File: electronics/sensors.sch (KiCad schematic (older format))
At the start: 11 parts, among them U3 MPU-9250, U4 MS5611-01BA, U5 VL53L0X

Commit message: Use wifi for telemetry
Cleanup schematic
Use ESP12E (wifi) for telemetry instead of NRF24
Reannotate & replot pdf
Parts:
- renumbered C14 to C16, C15 to C17, C17 to C20, C16 to C21, R18 to R16, U3 to U4, U4 to U5, U5 to U6
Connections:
- net MPU9250_CS renamed IMU_CS
- net MPU9250_INT renamed IMU_INT
- net SPI1_MISO renamed IMU_MISO
- net SPI1_MOSI renamed IMU_MOSI
- net SPI1_SCK renamed IMU_SCK
- net ST_VL53L0X_GPIO1 renamed TOF_GPIO1
- net ST_VL53L0X_XSHUT renamed TOF_XSHUT
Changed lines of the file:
@@
 $Descr A4 11693 8268
 encoding utf-8
-Sheet 2 4
+Sheet 2 3
 Title "Speedy the nanocopter"
-Date "2016-06-04"
-Rev "1E"
+Date "2016-06-24"
+Rev "1F"
 Comp "Salah-Eddine Missri"
 Comment1 "License: CC-BY 4.0"
@@
 	1    0    0    -1
 $EndComp
-Text HLabel 3425 2125 2    39   Input ~ 0
-SPI1_SCK
-Text HLabel 3425 2225 2    39   Input ~ 0
-SPI1_MOSI
-Text HLabel 3425 2375 2    39   Input ~ 0
-SPI1_MISO
-Text HLabel 3425 2525 2    39   Input ~ 0
-MPU9250_CS
-Text HLabel 3425 2675 2    39   Input ~ 0
-MPU9250_INT
-$Comp
-L MS5611-01BA U4
+Text HLabel 3375 2125 2    39   Input ~ 0
+IMU_SCK
+Text HLabel 3375 2225 2    39   Input ~ 0
+IMU_MOSI
+Text HLabel 3375 2375 2    39   Input ~ 0
+IMU_MISO
+Text HLabel 3375 2525 2    39   Input ~ 0
+IMU_CS
+Text HLabel 3375 2675 2    39   Input ~ 0
+IMU_INT
+$Comp
+L MS5611-01BA U5
 U 1 1 553861F3
 P 5975 2525
-F 0 "U4" H 6325 2925 50  0000 C CNN
+F 0 "U5" H 6325 2925 50  0000 C CNN
 F 1 "MS5611-01BA" H 5825 2925 50  0000 C CNN
 F 2 "_sensors:_MS5611-01BA" H 5975 2525 50  0001 C CNN
@@
 NoConn ~ 1775 2425
 $Comp
-L C_Small C14
+L C_Small C16
 U 1 1 554288B9
 P 1275 2025
-F 0 "C14" H 1285 2095 50  0000 L CNN
+F 0 "C16" H 1285 2095 50  0000 L CNN
 F 1 "0.1uF" H 1285 1945 50  0000 L CNN
 F 2 "_std:_0402" H 1275 2025 60  0001 C CNN
@@
 $EndComp
 $Comp
-L C_Small C15
+L C_Small C17
 U 1 1 55428A44
 P 1525 2025
-F 0 "C15" H 1535 2095 50  0000 L CNN
+F 0 "C17" H 1535 2095 50  0000 L CNN
 F 1 "10nF" H 1535 1945 50  0000 L CNN
 F 2 "_std:_0402" H 1525 2025 60  0001 C CNN
@@
 $EndComp
 $Comp
-L C_Small C16
+L C_Small C21
 U 1 1 55428B56
 P 3750 2875
-F 0 "C16" H 3760 2945 50  0000 L CNN
+F 0 "C21" H 3760 2945 50  0000 L CNN
 F 1 "0.1uF" H 3760 2795 50  0000 L CNN
 F 2 "_std:_0402" H 3750 2875 60  0001 C CNN
@@
 $EndComp
 $Comp
-L C_Small C17
+L C_Small C20
 U 1 1 55428C9E
 P 4975 2575
-F 0 "C17" H 4985 2645 50  0000 L CNN
+F 0 "C20" H 4985 2645 50  0000 L CNN
 F 1 "0.1uF" H 4985 2495 50  0000 L CNN
 F 2 "_std:_0402" H 4975 2575 60  0001 C CNN
@@
 	3750 2775 3375 2775
 Wire Wire Line
-	3425 2375 3375 2375
-Wire Wire Line
-	3425 2525 3375 2525
-Wire Wire Line
-	3425 2225 3375 2225
-Wire Wire Line
-	3425 2125 3375 2125
-Wire Wire Line
-	3425 2675 3375 2675
-Wire Wire Line
-	9900 2750 10250 2750
-Wire Wire Line
-	9900 2650 10250 2650
+	3375 2375 3375 2375
+Wire Wire Line
+	3375 2525 3375 2525
+Wire Wire Line
+	3375 2225 3375 2225
+Wire Wire Line
+	3375 2125 3375 2125
+Wire Wire Line
+	3375 2675 3375 2675
+Wire Wire Line
+	9900 2750 9900 2750
+Wire Wire Line
+	9900 2650 9900 2650
 Wire Wire Line
 	4975 2675 4975 2750
@@
 	5175 2425 5175 2325
 Wire Wire Line
-	6775 2425 6725 2425
-Wire Wire Line
-	6725 2325 6775 2325
+	6725 2425 6725 2425
+Wire Wire Line
+	6725 2325 6725 2325
 Wire Wire Line
 	6725 2725 6775 2725
@@
 Text Notes 3350 950  0    60   ~ 0
 IMU 10dof
-Text HLabel 6775 2325 2    39   Input ~ 0
+Text HLabel 6725 2325 2    39   Input ~ 0
 I2C1_SCL
-Text HLabel 6775 2425 2    39   Input ~ 0
+Text HLabel 6725 2425 2    39   Input ~ 0
 I2C1_SDA
-Text HLabel 10250 2750 2    39   Input ~ 0
+Text HLabel 9900 2750 2    39   Input ~ 0
 I2C1_SCL
-Text HLabel 10250 2650 2    39   Input ~ 0
+Text HLabel 9900 2650 2    39   Input ~ 0
 I2C1_SDA
 NoConn ~ 1775 3225
@@
 	3375 2875 3625 2875
 $Comp
-L MPU-9250 U3
+L MPU-9250 U4
 U 1 1 56ACAF9A
 P 2575 2525
-F 0 "U3" H 2575 3462 60  0000 C CNN
+F 0 "U4" H 2575 3462 60  0000 C CNN
 F 1 "MPU-9250" H 2575 3356 60  0000 C CNN
 F 2 "_sensors:_MPU-9XX0" H 2575 3125 60  0001 C CNN
@@
 VCCA
 $Comp
-L VL53L0X U5
+L VL53L0X U6
 U 1 1 57532742
 P 9300 2750
-F 0 "U5" H 9300 3437 60  0000 C CNN
+F 0 "U6" H 9300 3437 60  0000 C CNN
 F 1 "VL53L0X" H 9300 3331 60  0000 C CNN
 F 2 "_sensors:ST-VL53L0X" H 9350 2700 60  0001 C CNN
@@
 Connection ~ 8075 2350
 Text HLabel 10250 2450 2    39   Input ~ 0
-ST_VL53L0X_GPIO1
+TOF_GPIO1
 Text HLabel 10250 2350 2    39   Input ~ 0
-ST_VL53L0X_XSHUT
+TOF_XSHUT
 Wire Wire Line
 	9900 2350 10250 2350
@@
 Connection ~ 9925 2350
 $Comp
-L R_Small R18
+L R_Small R16
 U 1 1 575376D4
 P 10175 1950
-F 0 "R18" H 10234 1996 50  0000 L CNN
+F 0 "R16" H 10234 1996 50  0000 L CNN
 F 1 "10k" H 10234 1905 50  0000 L CNN
 F 2 "_std:_0402" H 10175 1950 50  0001 C CNN

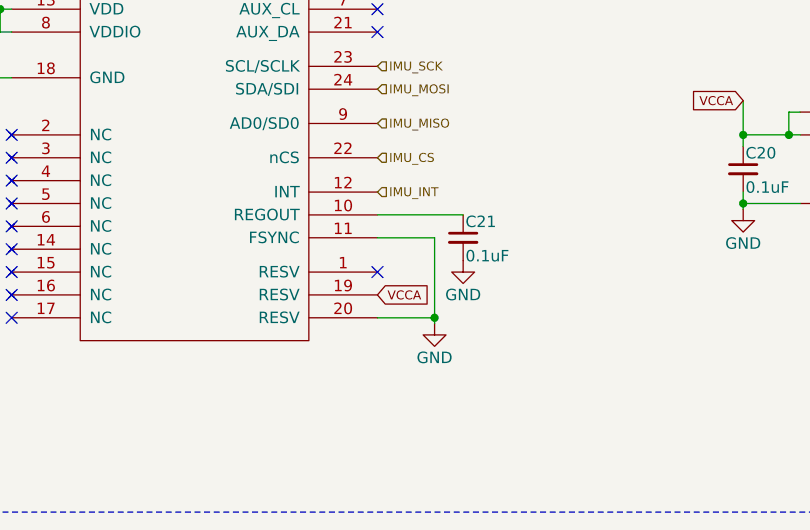
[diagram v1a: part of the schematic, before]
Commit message: Update with small corrections
Decrease LED resistor values
Fix NUF2042 name
Fix MPU9250 wiring (contradictory datasheet)
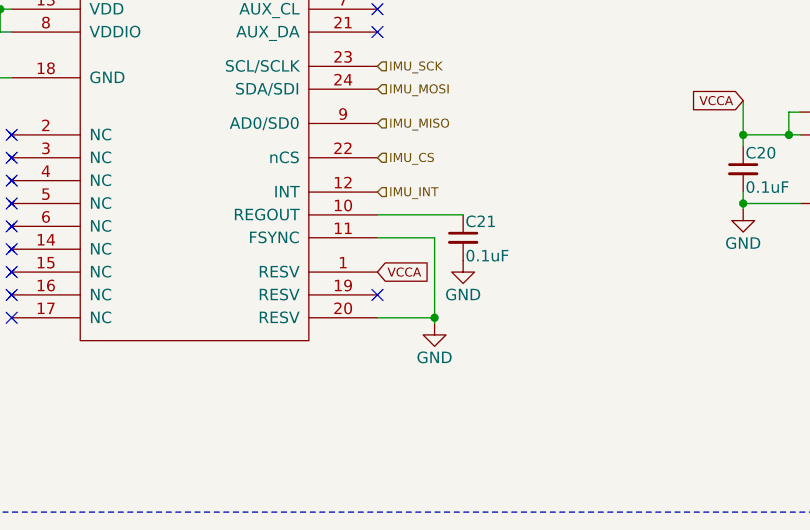
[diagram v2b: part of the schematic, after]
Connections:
- net VCCA: now also U4.1 (RESV); no longer U4.19 (RESV)
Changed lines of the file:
@@
 Wire Notes Line
 	475  4075 11225 4075
-NoConn ~ 3375 3025
+NoConn ~ 3375 3125
 Wire Wire Line
 	3375 2875 3625 2875
@@
 	3375 3225 3625 3225
 Connection ~ 3625 3225
-Text GLabel 3375 3125 2    39   Input ~ 0
+Text GLabel 3375 3025 2    39   Input ~ 0
 VCCA
 $Comp
